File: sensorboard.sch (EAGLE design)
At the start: 43 parts, among them U1 LM1117MP-3.3, U2 LM324D

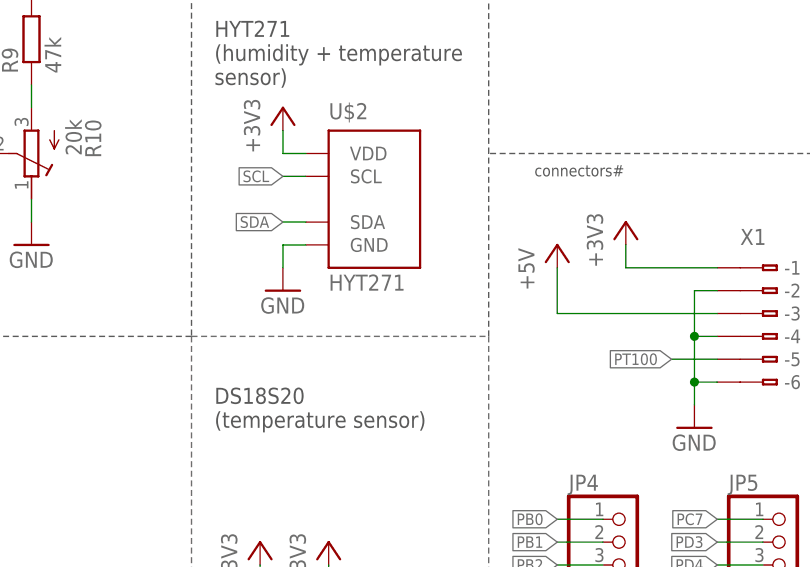
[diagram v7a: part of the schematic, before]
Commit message: changed HYT271 from SMD to THT
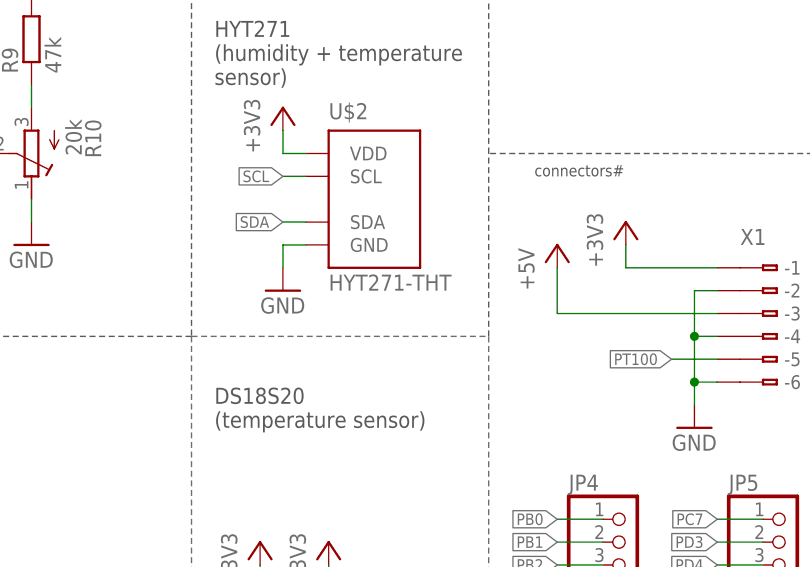
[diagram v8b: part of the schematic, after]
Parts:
- U$2: value HYT271 -> HYT271-THT; device humidity:HYT271 -> humidity:HYT271-THT
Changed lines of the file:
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@@
 <part name="+3V10" library="supply1" deviceset="+3V3" device=""/>
 <part name="P+3" library="supply1" deviceset="+5V" device=""/>
-<part name="U$2" library="humidity" deviceset="HYT271" device=""/>
+<part name="U$2" library="humidity" deviceset="HYT271-THT" device=""/>
 <part name="+3V11" library="supply1" deviceset="+3V3" device=""/>
 <part name="GND12" library="supply1" deviceset="GND" device=""/>
@@
 <instance part="+3V10" gate="G$1" x="177.8" y="71.12"/>
 <instance part="P+3" gate="1" x="170.18" y="68.58"/>
-<instance part="U$2" gate="A" x="149.86" y="73.66"/>
+<instance part="U$2" gate="G$1" x="149.86" y="73.66"/>
 <instance part="+3V11" gate="G$1" x="139.7" y="83.82"/>
 <instance part="GND12" gate="1" x="139.7" y="63.5"/>
@@
 </segment>
 <segment>
-<pinref part="U$2" gate="A" pin="GND"/>
+<pinref part="U$2" gate="G$1" pin="GND"/>
 <pinref part="GND12" gate="1" pin="GND"/>
 <wire x1="142.24" y1="68.58" x2="139.7" y2="68.58" width="0.1524" layer="91"/>
@@
 </segment>
 <segment>
-<pinref part="U$2" gate="A" pin="VDD"/>
+<pinref part="U$2" gate="G$1" pin="VDD"/>
 <pinref part="+3V11" gate="G$1" pin="+3V3"/>
 <wire x1="142.24" y1="78.74" x2="139.7" y2="78.74" width="0.1524" layer="91"/>
@@
 </segment>
 <segment>
-<pinref part="U$2" gate="A" pin="SDA"/>
+<pinref part="U$2" gate="G$1" pin="SDA"/>
 <wire x1="142.24" y1="71.12" x2="139.7" y2="71.12" width="0.1524" layer="91"/>
 <label x="139.7" y="71.12" size="1.27" layer="95" rot="R180" xref="yes"/>
@@
 </segment>
 <segment>
-<pinref part="U$2" gate="A" pin="SCL"/>
+<pinref part="U$2" gate="G$1" pin="SCL"/>
 <wire x1="142.24" y1="76.2" x2="139.7" y2="76.2" width="0.1524" layer="91"/>
 <label x="139.7" y="76.2" size="1.27" layer="95" rot="R180" xref="yes"/>
